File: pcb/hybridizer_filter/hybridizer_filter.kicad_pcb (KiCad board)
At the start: 2 copper layers, 85.6 x 132.2 mm, 126 parts, among them P1 HEADER_02X07_SMD, P2 HEADER_02X05_SMD, P3 HEADER_02X05_SMD, U1 VA, U11 VA, U13 VA, U15 DRV103, U16 DRV103, U17 DRV103, U18 DRV103, U19 DRV103, U20 DRV103, U21 DRV103, U22 DRV103, U23 OA, U24 OA, U25 OA, U26 OA, U27 OA, U28 OA, U29 OA, U3 VA, U5 VA, U7 VA, U9 VA

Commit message: Progress towards hybridizer_filter v1.0.
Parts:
- removed C34, C35, C36, C37: 10nF, hybridizer_filter:SM0402
- removed C38, C39, C40, C41, C42, C43, C44: 0.1uF, hybridizer_filter:SM1210
- removed C45, C47: 22uF, hybridizer_filter:SM1210_POL
- removed C46, C48: 10uF, hybridizer_filter:SM1210
- removed CLEARANCE_HOLE_1, CLEARANCE_HOLE_2, CLEARANCE_HOLE_3, CLEARANCE_HOLE_4, CLEARANCE_HOLE_5, CLEARANCE_HOLE_6: clearance_hole, hybridizer_filter:clearance_hole
- removed D10, D11, D12, D13, D14, D15, D16, D9: diode_schottky_20V_1A, hybridizer_filter:SM0805_POL
- removed D2, D3, D4, D5, D6, D7, D8: LED_0805, hybridizer_filter:LED0805
- removed MOUNTING_HOLE_1, MOUNTING_HOLE_2, MOUNTING_HOLE_3, MOUNTING_HOLE_4, MOUNTING_HOLE_5, MOUNTING_HOLE_6: mounting_hole, hybridizer_filter:mounting_hole
- removed REF**, VALVE_HOLE_1, VALVE_HOLE_2, VALVE_HOLE_3, VALVE_HOLE_4, VALVE_HOLE_5, VALVE_HOLE_6: valve_hole, hybridizer_filter:valve_hole
- removed S1: HEADER_01X02_SMD_N, hybridizer_filter:Header_2_Pin_SMD_N
- removed S2, S3, S4, S5, S6, S7: HEADER_01X02_SMD, hybridizer_filter:Header_2_Pin_SMD
- removed S8: LEE_VALVE_PLUG_IN, hybridizer_filter:LEE_VALVE_PLUG_IN
- removed U16, U17, U18, U19, U20, U21, U22: DRV103, hybridizer_filter:SOIC_8
- removed U23, U24, U25, U26, U27, U28, U29: OA, hybridizer_filter:SOT-23-3
- added C11: 0.1uF, hybridizer_filter:SM0805, B.Cu at (112.6, 90.6)
- added C12: 0.1uF, hybridizer_filter:SM0805, B.Cu at (112.6, 100.7)
- added C14: 0.1uF, hybridizer_filter:SM0805, B.Cu at (112.6, 113.4)
- added C15: 0.1uF, hybridizer_filter:SM0805, B.Cu at (112.6, 116.0)
- added C17: 0.1uF, hybridizer_filter:SM0805, B.Cu at (112.6, 128.7)
- added C18: 0.1uF, hybridizer_filter:SM0805, B.Cu at (112.6, 138.8)
- added C2: 22uF, hybridizer_filter:SM1210_POL, B.Cu at (116.5, 152.8)
- added C20: 0.1uF, hybridizer_filter:SM0805, B.Cu at (138.0, 62.6)
- added C21: 0.1uF, hybridizer_filter:SM0805, B.Cu at (138.0, 65.2)
- added C3: 10uF, hybridizer_filter:SM1210, B.Cu at (122.8, 152.8)
- added C5: 10uF, hybridizer_filter:SM1210, B.Cu at (122.8, 146.4)
- added C6: 0.1uF, hybridizer_filter:SM0805, B.Cu at (117.7, 62.6)
- added C8: 0.1uF, hybridizer_filter:SM0805, B.Cu at (112.6, 75.3)
- added C9: 0.1uF, hybridizer_filter:SM0805, B.Cu at (112.6, 77.9)
- added MH1: mounting_hole, hybridizer_filter:mounting_hole, F.Cu at (111.4, 57.5)
- added MH2: mounting_hole, hybridizer_filter:mounting_hole, F.Cu at (162.2, 57.5)
- added MH3: mounting_hole, hybridizer_filter:mounting_hole, F.Cu at (111.4, 159.1)
- added MH4: mounting_hole, hybridizer_filter:mounting_hole, F.Cu at (162.2, 159.1)
- added P4: HEADER_02X05_SMD, hybridizer_filter:HEADER_02x05_SMD, F.Cu at (117.7, 89.3)
- added P5: HEADER_02X05_SMD, hybridizer_filter:HEADER_02x05_SMD, F.Cu at (155.8, 89.3)
- added R1: 1k, hybridizer_filter:SM0805, F.Cu at (144.4, 151.5)
- added R2: 3.16M, hybridizer_filter:SM0805, B.Cu at (117.7, 56.3)
- added R3: 3.16M, hybridizer_filter:SM0805, B.Cu at (134.2, 63.9)
- added R32: 49.9k, hybridizer_filter:SM0805, B.Cu at (138.0, 58.8)
- added R33: 42.2k, hybridizer_filter:SM0805, B.Cu at (154.6, 57.5)
- added R34: 3.16M, hybridizer_filter:SM0805, B.Cu at (143.1, 69.0)
- added R35: 3.16M, hybridizer_filter:SM0805, B.Cu at (159.6, 76.6)
- added R36: 49.9k, hybridizer_filter:SM0805, B.Cu at (143.1, 71.5)
- added R37: 42.2k, hybridizer_filter:SM0805, B.Cu at (159.6, 70.2)
- added R38: 3.16M, hybridizer_filter:SM0805, B.Cu at (143.1, 81.7)
- added R39: 3.16M, hybridizer_filter:SM0805, B.Cu at (159.6, 89.3)
- added R4: 49.9k, hybridizer_filter:SM0805, B.Cu at (117.7, 58.8)
- added R40: 49.9k, hybridizer_filter:SM0805, B.Cu at (143.1, 84.2)
- added R41: 42.2k, hybridizer_filter:SM0805, B.Cu at (159.6, 82.9)
- added R42: 3.16M, hybridizer_filter:SM0805, B.Cu at (143.1, 94.4)
- added R43: 3.16M, hybridizer_filter:SM0805, B.Cu at (159.6, 102.0)
- added R44: 49.9k, hybridizer_filter:SM0805, B.Cu at (143.1, 96.9)
- added R45: 42.2k, hybridizer_filter:SM0805, B.Cu at (159.6, 95.6)
- added R46: 3.16M, hybridizer_filter:SM0805, B.Cu at (143.1, 107.1)
- added R47: 3.16M, hybridizer_filter:SM0805, B.Cu at (159.6, 114.7)
- added R48: 49.9k, hybridizer_filter:SM0805, B.Cu at (143.1, 109.6)
- added R49: 42.2k, hybridizer_filter:SM0805, B.Cu at (159.6, 108.3)
- added R5: 42.2k, hybridizer_filter:SM0805, B.Cu at (134.2, 57.5)
- added R50: 3.16M, hybridizer_filter:SM0805, B.Cu at (143.1, 119.8)
- added R51: 3.16M, hybridizer_filter:SM0805, B.Cu at (159.6, 127.4)
- added R52: 49.9k, hybridizer_filter:SM0805, B.Cu at (143.1, 122.3)
- added R53: 42.2k, hybridizer_filter:SM0805, B.Cu at (159.6, 121.0)
- added R54: 3.16M, hybridizer_filter:SM0805, B.Cu at (143.1, 132.5)
- added R55: 3.16M, hybridizer_filter:SM0805, B.Cu at (159.6, 140.1)
- added R56: 49.9k, hybridizer_filter:SM0805, B.Cu at (143.1, 135.0)
- added R57: 42.2k, hybridizer_filter:SM0805, B.Cu at (159.6, 133.7)
- added R6: 3.16M, hybridizer_filter:SM0805, B.Cu at (112.6, 69.0)
- added R7: 3.16M, hybridizer_filter:SM0805, B.Cu at (129.2, 76.6)
- added U10: UAF42, hybridizer_filter:SOIC_16, B.Cu at (152.0, 72.8)
- added U12: UAF42, hybridizer_filter:SOIC_16, B.Cu at (152.0, 98.2)
- added U14: UAF42, hybridizer_filter:SOIC_16, B.Cu at (152.0, 123.6)
- added U2: UAF42, hybridizer_filter:SOIC_16, B.Cu at (126.6, 60.1)
- added U4: UAF42, hybridizer_filter:SOIC_16, B.Cu at (121.5, 85.5)
- added U6: UAF42, hybridizer_filter:SOIC_16, B.Cu at (121.5, 110.9)
- added U8: UAF42, hybridizer_filter:SOIC_16, B.Cu at (121.5, 136.3)
- C1: value 0.1uF -> 10uF; moved to B.Cu
- C10, C13, C16, C19, C7: footprint hybridizer_filter:SM1210 -> hybridizer_filter:SM0805; moved to B.Cu
- C22, C23, C24, C25, C30, C31, C32, C33: value 1uF -> 0.1uF; footprint hybridizer_filter:SM0805_POL -> hybridizer_filter:SM0805; moved to B.Cu
- C26, C27, C28, C29: value 10nF -> 0.1uF; footprint hybridizer_filter:SM0402 -> hybridizer_filter:SM0805; moved to B.Cu
- C4: value 0.1uF -> 22uF; footprint hybridizer_filter:SM1210 -> hybridizer_filter:SM1210_POL; moved to B.Cu
- P1: value HEADER_02X07_SMD -> PWR_JACK_2.1x5.5; footprint hybridizer_filter:HEADER_02x07_SMD -> hybridizer_filter:DCJACK_2PIN_HIGHCURRENT
- R10, R11, R14, R15: value 300 -> 3.16M; footprint hybridizer_filter:SM0402 -> hybridizer_filter:SM0805; moved to B.Cu
- R12, R8: value 300 -> 49.9k; footprint hybridizer_filter:SM0402 -> hybridizer_filter:SM0805; moved to B.Cu
- R13, R9: value 300 -> 42.2k; footprint hybridizer_filter:SM0402 -> hybridizer_filter:SM0805; moved to B.Cu
- R16, R20, R24, R28: value 205k -> 49.9k; footprint hybridizer_filter:SM0402 -> hybridizer_filter:SM0805; moved to B.Cu
- R17, R21, R25, R29: value 110k -> 42.2k; footprint hybridizer_filter:SM0402 -> hybridizer_filter:SM0805; moved to B.Cu
- R18, R22, R26, R30: value 205k -> 3.16M; footprint hybridizer_filter:SM0402 -> hybridizer_filter:SM0805; moved to B.Cu
- R19, R23, R27: value 110k -> 3.16M; footprint hybridizer_filter:SM0402 -> hybridizer_filter:SM0805; moved to B.Cu
- R31: value 137k -> 3.16M; footprint hybridizer_filter:SM0402 -> hybridizer_filter:SM0805; moved to B.Cu
- U1: value VA -> CONV_+9V_-9V_SIP8; footprint hybridizer_filter:SOT-23-3 -> hybridizer_filter:SIP8_RECOM; moved to F.Cu
- U11, U13, U3, U5, U7, U9: value VA -> UAF42; footprint hybridizer_filter:SOT-23-3 -> hybridizer_filter:SOIC_16
- U15: value DRV103 -> UAF42; footprint hybridizer_filter:SOIC_8 -> hybridizer_filter:SOIC_16; moved to B.Cu
- moved C4 112.0 mm to (116.5, 146.4), turned to 90 degrees
- moved P1 105.3 mm to (136.8, 163.0), turned to 180 degrees
- moved C30 103.3 mm to (143.1, 126.1), turned to 180 degrees
- moved R19 93.4 mm to (129.2, 114.7)
- moved C27 90.2 mm to (143.1, 103.3), turned to 0 degrees
- moved C31 89.8 mm to (143.1, 128.7)
- moved R27 86.8 mm to (129.2, 140.1), turned to 270 degrees
- moved R25 86.2 mm to (129.2, 121.0)
- moved R24 84.1 mm to (112.6, 122.3), turned to 180 degrees
- moved C28 83.8 mm to (143.1, 113.4), turned to 180 degrees
- moved C32 83.2 mm to (143.1, 138.8), turned to 180 degrees
- moved R18 78.8 mm to (112.6, 107.1), turned to 0 degrees
- moved P3 77.1 mm to (155.8, 127.4)
- moved C13 77.0 mm to (112.6, 103.3), turned to 0 degrees
- moved U11 76.5 mm to (152.0, 85.5)
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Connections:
- C1 pad 1: +5V -> VAA
- C1 pad 2: GNDA -> GND
- C10 pad 1: +5V -> VDD
- C13 pad 1: +5V -> GNDA
- C13 pad 2: GNDA -> VEE
- C16 pad 1: +5V -> VDD
- C19 pad 1: +5V -> GNDA
- C19 pad 2: GNDA -> VEE
- C22 pad 1: VAA -> VDD
- C22 pad 2: GND -> GNDA
- C23 pad 1: VAA -> GNDA
- C23 pad 2: GND -> VEE
- C24 pad 1: VAA -> VDD
- C24 pad 2: GND -> GNDA
- C25 pad 1: VAA -> GNDA
- C25 pad 2: GND -> VEE
- C26 pad 1: Net-(C26-Pad1) -> VDD
- C26 pad 2: GND -> GNDA
- C27 pad 1: Net-(C27-Pad1) -> GNDA
- C27 pad 2: GND -> VEE
- C28 pad 1: Net-(C28-Pad1) -> VDD
- C28 pad 2: GND -> GNDA
- C29 pad 1: Net-(C29-Pad1) -> GNDA
- C29 pad 2: GND -> VEE
- C30 pad 1: VAA -> VDD
- C30 pad 2: GND -> GNDA
- C31 pad 1: VAA -> GNDA
- C31 pad 2: GND -> VEE
- C32 pad 1: VAA -> VDD
- C32 pad 2: GND -> GNDA
- C33 pad 1: VAA -> GNDA
- C33 pad 2: GND -> VEE
- C4 pad 1: +5V -> GNDA
- C4 pad 2: GNDA -> VEE
- C7 pad 1: +5V -> GNDA
- C7 pad 2: GNDA -> VEE
- P2 pad 1: +5V -> /Va
- P3 pad 1: Net-(P3-Pad1) -> /Va
- P3 pad 2: Net-(P3-Pad2) -> GNDA
- P3 pad 3: /A8 -> /A0_F
- P3 pad 4: /A9 -> /A1_F
- P3 pad 5: /A10 -> /A2_F
- P3 pad 6: /A11 -> /A3_F
- P3 pad 7: /A12 -> /A4_F
- P3 pad 8: /A13 -> /A5_F
- P3 pad 9: /A14 -> /A6_F
- R10 pad 1: /IO2 -> Net-(R10-Pad1)
- R11 pad 1: /IO3 -> Net-(R11-Pad1)
- R12 pad 1: /IO4 -> Net-(R12-Pad1)
- R12 pad 2: Net-(D5-Pad1) -> /A2
- R13 pad 1: /IO5 -> Net-(R13-Pad1)
- R13 pad 2: Net-(D6-Pad1) -> GNDA
- R14 pad 1: /IO6 -> Net-(R14-Pad1)
- R14 pad 2: Net-(D7-Pad1) -> Net-(R14-Pad2)
- R15 pad 1: /IO7 -> Net-(R15-Pad1)
- R15 pad 2: Net-(D8-Pad1) -> Net-(R15-Pad2)
- R16 pad 2: GND -> /A3
- R17 pad 2: GND -> GNDA
- R18 pad 2: GND -> Net-(R18-Pad2)
- R19 pad 2: GND -> Net-(R19-Pad2)
- R20 pad 2: GND -> /A4
- R21 pad 2: GND -> GNDA
- R22 pad 2: GND -> Net-(R22-Pad2)
- R23 pad 2: GND -> Net-(R23-Pad2)
- R24 pad 2: GND -> /A5
- R25 pad 2: GND -> GNDA
- R26 pad 2: GND -> Net-(R26-Pad2)
- R27 pad 2: GND -> Net-(R27-Pad2)
- R28 pad 2: GND -> /A6
- R29 pad 2: GND -> GNDA
- R30 pad 2: GND -> Net-(R30-Pad2)
- R31 pad 2: GND -> Net-(R31-Pad2)
- R8 pad 1: /IO0 -> Net-(R8-Pad1)
- R8 pad 2: Net-(D1-Pad1) -> /A1
- R9 pad 1: /IO1 -> Net-(R9-Pad1)
- R9 pad 2: Net-(D2-Pad1) -> GNDA
- U1 pad 1: +5V -> GND
- U1 pad 2: /A0 -> VAA
- U1 pad 3: GNDA -> (no net)
- U11 pad 1: +5V -> /A10_LP
- U11 pad 2: /A5 -> GNDA
- U11 pad 3: GNDA -> Net-(U11-Pad3)
- U13 pad 1: +5V -> /A12_LP
- U13 pad 2: /A6 -> GNDA
- U13 pad 3: GNDA -> Net-(U13-Pad3)
- U15 pad 1: Net-(R17-Pad1) -> /A14_LP
- U15 pad 2: Net-(C26-Pad1) -> GNDA
- U15 pad 3: Net-(R16-Pad1) -> Net-(U15-Pad3)
- U15 pad 4: GND -> Net-(R57-Pad1)
- U15 pad 5: /SH0 -> /A14_LP
- U15 pad 6: VAA -> /A14_F
- U15 pad 7: Net-(U15-Pad7) -> /A14_F
- U15 pad 8: /IO0 -> Net-(R55-Pad2)
- U3 pad 1: +5V -> /A1_LP
- U3 pad 2: /A1 -> GNDA
- U3 pad 3: GNDA -> Net-(U3-Pad3)
- U5 pad 1: +5V -> /A3_LP
- U5 pad 2: /A2 -> GNDA
- U5 pad 3: GNDA -> Net-(U5-Pad3)
- U7 pad 1: +5V -> /A5_LP
- U7 pad 2: /A3 -> GNDA
- U7 pad 3: GNDA -> Net-(U7-Pad3)
- U9 pad 1: +5V -> /A8_LP
- U9 pad 2: /A4 -> GNDA
- U9 pad 3: GNDA -> Net-(U9-Pad3)
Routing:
- net GND: track 487.3 -> 0.00 mm, vias 7 -> 0
- net VAA: track 408.7 -> 0.00 mm
- net GNDA: track 390.6 -> 0.00 mm, vias 15 -> 0
- net +5V: track 360.5 -> 0.00 mm, vias 16 -> 0
- net /IO1: track 161.5 -> 0.00 mm
- net /IO4: track 119.2 -> 0.00 mm
- net /A8: track 118.7 -> 0.00 mm, vias 1 -> 0
- net /A4: track 116.7 -> 0.00 mm, vias 1 -> 0
- net /IO2: track 113.8 -> 0.00 mm, vias 2 -> 0
- net /A14: track 102.6 -> 0.00 mm, vias 1 -> 0
- net /IO3: track 100.0 -> 0.00 mm, vias 2 -> 0
- net /IO0: track 93.9 -> 0.00 mm, vias 3 -> 0
- net /A1: track 89.2 -> 0.00 mm, vias 1 -> 0
- net /IO5: track 76.5 -> 0.00 mm, vias 2 -> 0
- net /A0: track 73.8 -> 0.00 mm, vias 1 -> 0
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- removed copper zone on F.Cu, net GND
- removed copper zone on B.Cu, net GNDA
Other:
- board size 85.6 x 132.2 mm -> 58.4 x 109.2 mm
- board text added: "9-36VDC"
- board text added: "A0-A6"
- board text added: "A8-A14"
- board text added: "Filtered OUT"
- board text added: "Unfiltered IN"
- board text added: "hybridizer_filter Janelia Research Campus 07/2015 version 1.0"
- board text removed: "0"
- board text removed: "1"
- board text removed: "2"
- board text removed: "3"
- board text removed: "4"
- board text removed: "5"
- board text removed: "6"
- board text removed: "7"
- board text removed: "hybridizer_filter Janelia Research Campus 06/2015 version 1.2 J005165"

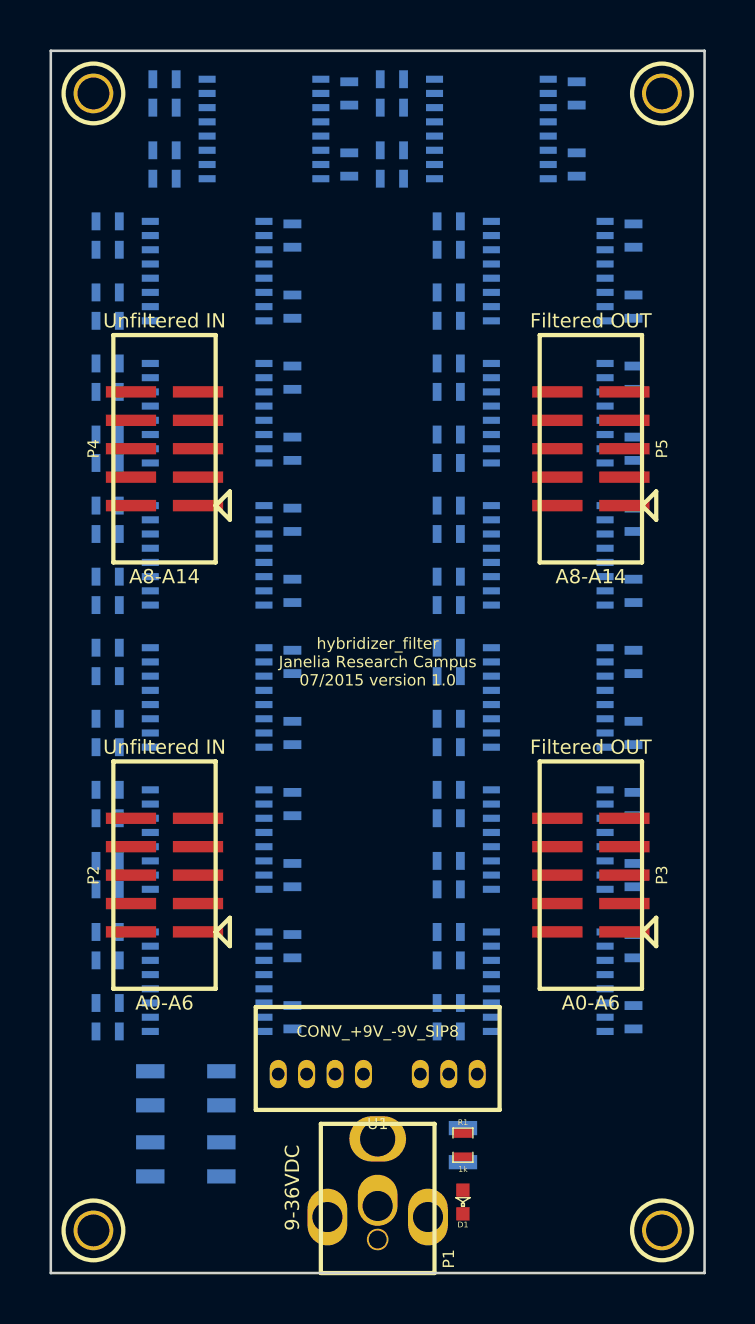
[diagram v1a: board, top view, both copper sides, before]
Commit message: Added auto traces to the board.
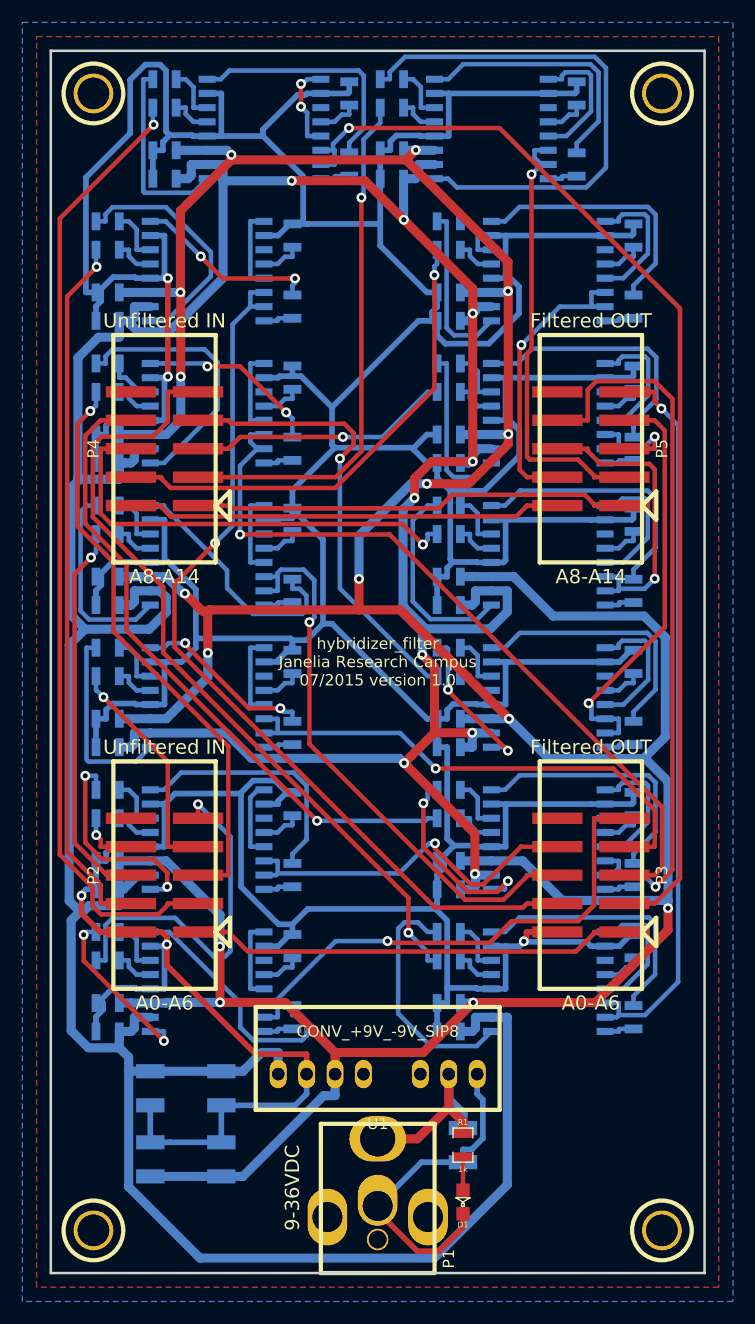
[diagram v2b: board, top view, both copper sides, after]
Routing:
- net GNDA: track 0.00 -> 627.9 mm, vias 0 -> 5
- net VEE: track 0.00 -> 387.0 mm, vias 0 -> 9
- net VDD: track 0.00 -> 365.3 mm, vias 0 -> 15
- net /A0_F: track 0.00 -> 99.4 mm, vias 0 -> 1
- net /A0: track 0.00 -> 86.3 mm, vias 0 -> 1
- net /A1_F: track 0.00 -> 80.9 mm, vias 0 -> 1
- net /A14: track 0.00 -> 72.2 mm, vias 0 -> 1
- net /A2_F: track 0.00 -> 68.5 mm, vias 0 -> 1
- net /A14_F: track 0.00 -> 66.4 mm, vias 0 -> 1
- net /A13_F: track 0.00 -> 65.6 mm, vias 0 -> 1
- net /A1: track 0.00 -> 63.5 mm, vias 0 -> 1
- net /A13: track 0.00 -> 58.5 mm, vias 0 -> 1
- net /A2: track 0.00 -> 52.2 mm, vias 0 -> 1
- net /A3_F: track 0.00 -> 51.5 mm, vias 0 -> 1
- net Net-(R30-Pad1): track 0.00 -> 47.1 mm
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- added copper zone on B.Cu, net GNDA
- added copper zone on F.Cu, net GNDA
